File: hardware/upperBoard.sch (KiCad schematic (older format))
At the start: 23 parts, among them J1 Program interface, J2 Conn_02x10_Odd_Even, Q1 MMBT3904, Q2 MMBT3904, SW1 Reset, SW2 Prog, U1 ESP-12F, U2 A2982, U3 MCP23017_SO, U4 A2982

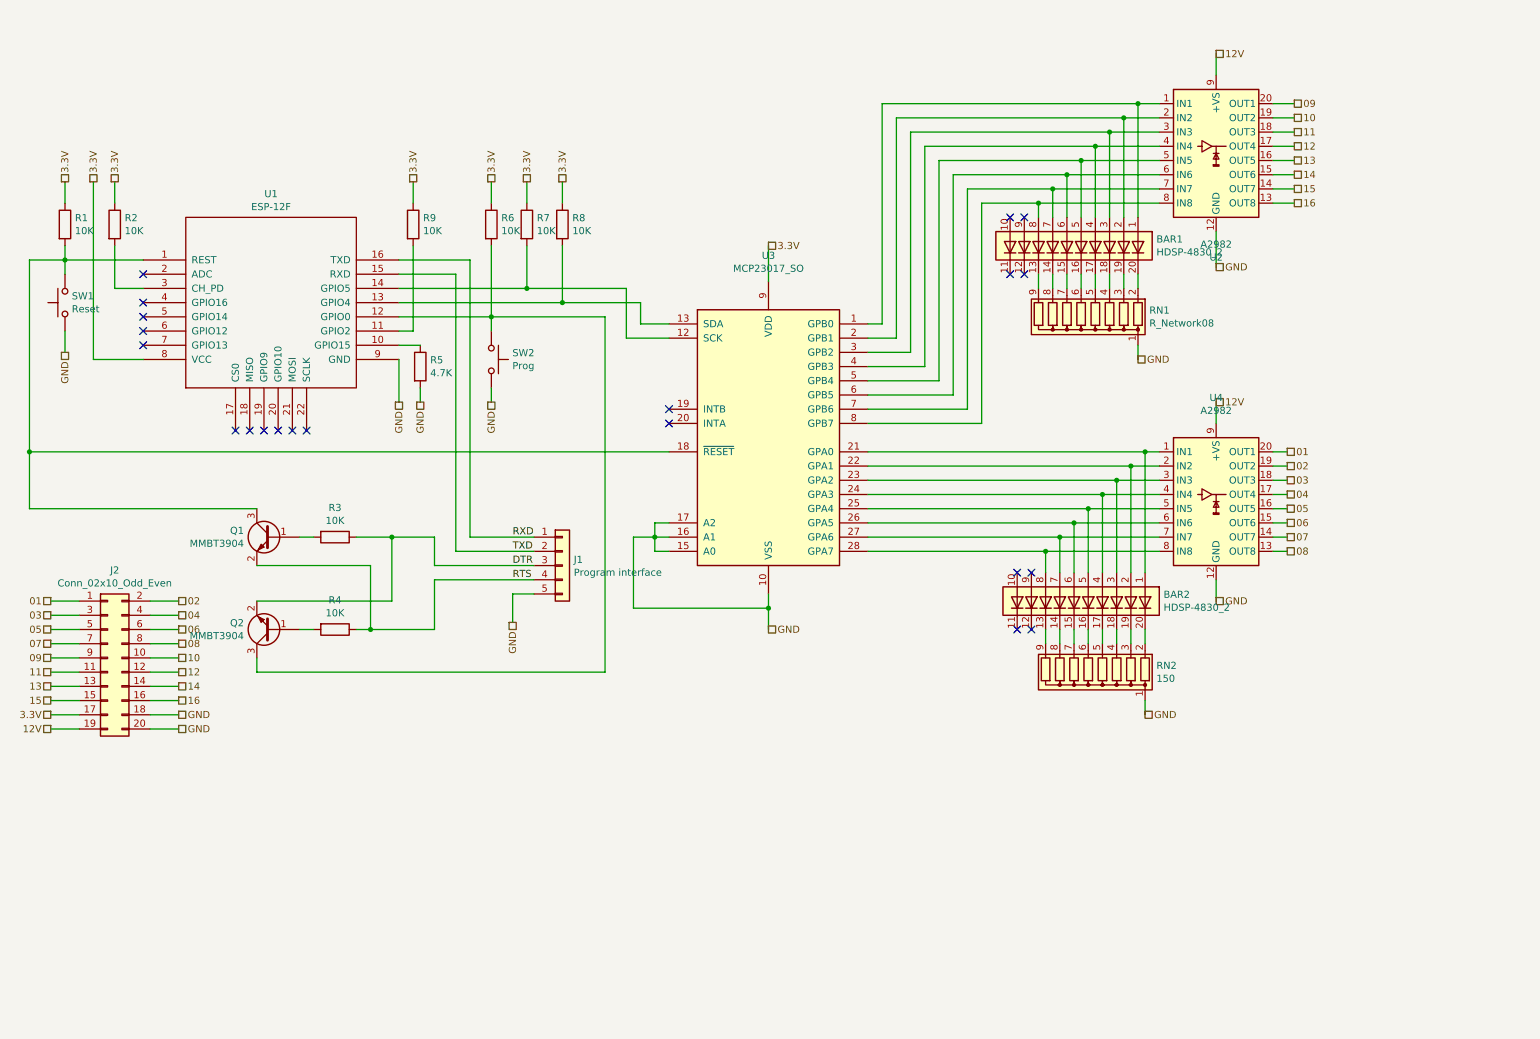
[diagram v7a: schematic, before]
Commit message: lower board fixes and started with upper printed circuit board
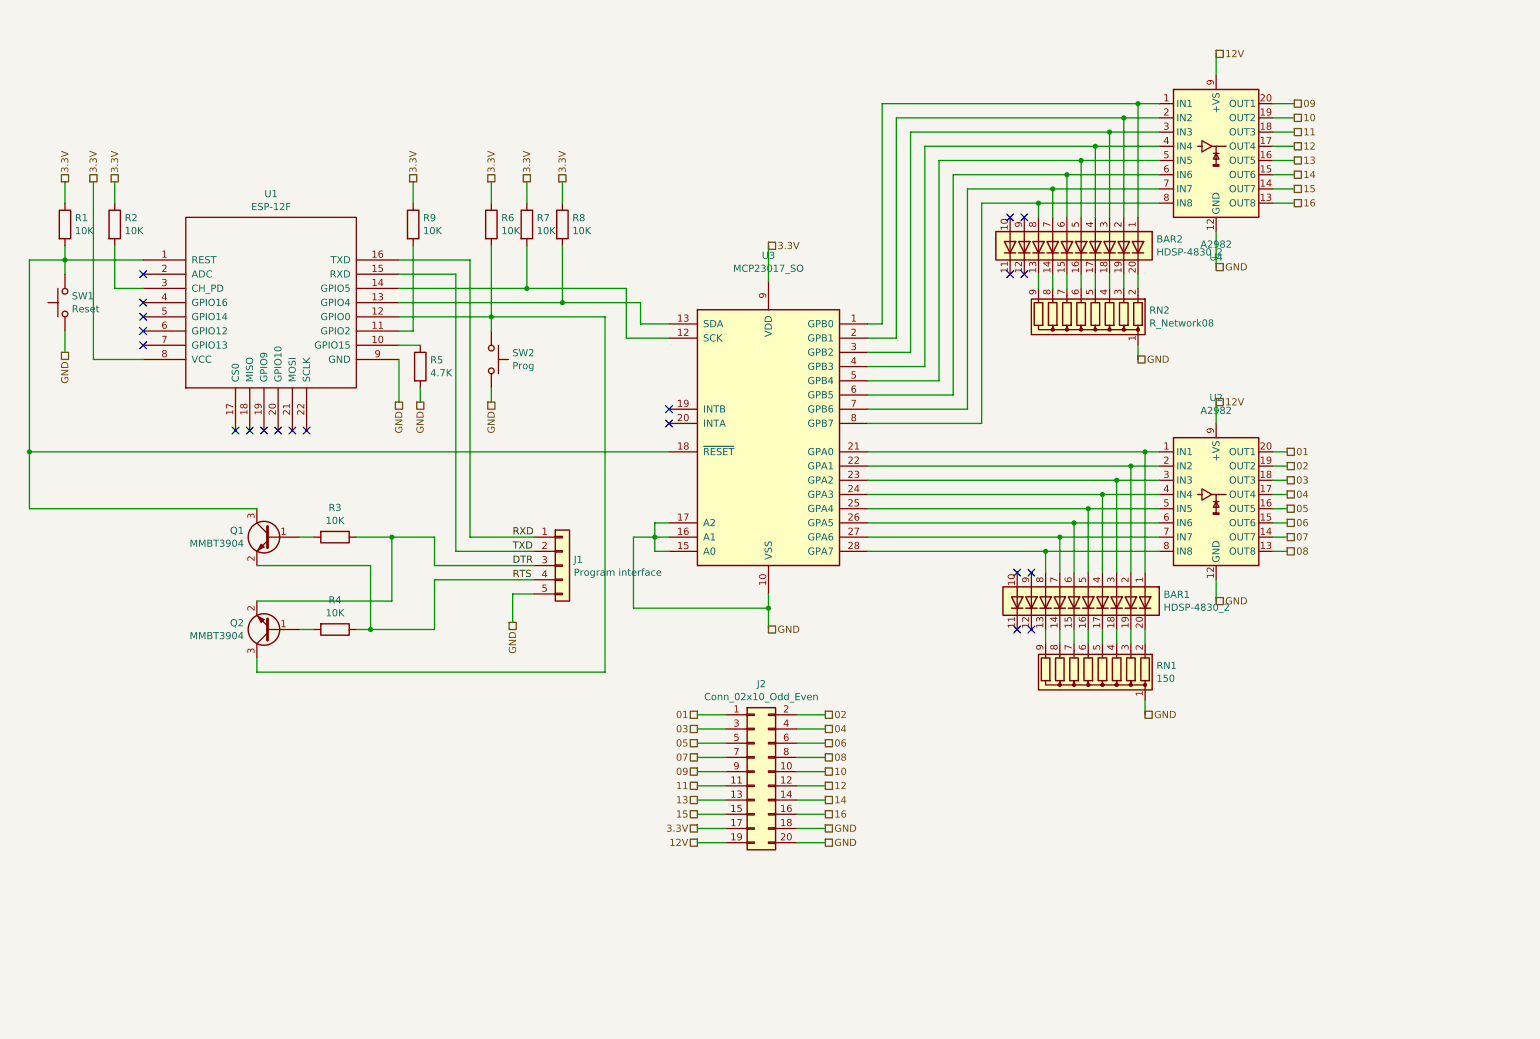
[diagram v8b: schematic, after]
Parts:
- BAR1: renamed from BAR2; footprint Display:HDSP-4830 -> Package_DIP:DIP-20_W7.62mm_LongPads
- BAR2: renamed from BAR1; footprint Display:HDSP-4830 -> Package_DIP:DIP-20_W7.62mm_Socket_LongPads
- J2: footprint (none) -> Connector_PinHeader_2.54mm:PinHeader_2x10_P2.54mm_Vertical
- renumbered RN2 to RN1, RN1 to RN2, U4 to U2, U2 to U4
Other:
- moved on the sheet: J2
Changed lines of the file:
@@
 Wire Wire Line
 	3300 2600 4450 2600
-Text HLabel 850  5500 0    50   UnSpc ~ 0
-3.3V
-Text HLabel 1750 5500 2    50   UnSpc ~ 0
+Text HLabel 5400 6300 0    50   UnSpc ~ 0
+3.3V
+Text HLabel 6300 6300 2    50   UnSpc ~ 0
 GND
 Text HLabel 3950 3300 3    50   UnSpc ~ 0
@@
 Text HLabel 4450 1750 1    50   UnSpc ~ 0
 3.3V
-Text HLabel 850  5400 0    50   UnSpc ~ 0
+Text HLabel 5400 6200 0    50   UnSpc ~ 0
 15
-Text HLabel 850  5300 0    50   UnSpc ~ 0
+Text HLabel 5400 6100 0    50   UnSpc ~ 0
 13
-Text HLabel 850  5200 0    50   UnSpc ~ 0
+Text HLabel 5400 6000 0    50   UnSpc ~ 0
 11
-Text HLabel 850  5100 0    50   UnSpc ~ 0
+Text HLabel 5400 5900 0    50   UnSpc ~ 0
 09
-Text HLabel 850  5000 0    50   UnSpc ~ 0
+Text HLabel 5400 5800 0    50   UnSpc ~ 0
 07
-Text HLabel 850  4900 0    50   UnSpc ~ 0
+Text HLabel 5400 5700 0    50   UnSpc ~ 0
 05
-Text HLabel 850  4800 0    50   UnSpc ~ 0
+Text HLabel 5400 5600 0    50   UnSpc ~ 0
 03
-Text HLabel 850  4700 0    50   UnSpc ~ 0
+Text HLabel 5400 5500 0    50   UnSpc ~ 0
 01
-Text HLabel 1750 5400 2    50   UnSpc ~ 0
+Text HLabel 6300 6200 2    50   UnSpc ~ 0
 16
-Text HLabel 1750 5300 2    50   UnSpc ~ 0
+Text HLabel 6300 6100 2    50   UnSpc ~ 0
 14
-Text HLabel 1750 5200 2    50   UnSpc ~ 0
+Text HLabel 6300 6000 2    50   UnSpc ~ 0
 12
-Text HLabel 1750 5100 2    50   UnSpc ~ 0
+Text HLabel 6300 5900 2    50   UnSpc ~ 0
 10
-Text HLabel 1750 5000 2    50   UnSpc ~ 0
+Text HLabel 6300 5800 2    50   UnSpc ~ 0
 08
-Text HLabel 1750 4900 2    50   UnSpc ~ 0
+Text HLabel 6300 5700 2    50   UnSpc ~ 0
 06
-Text HLabel 1750 4800 2    50   UnSpc ~ 0
+Text HLabel 6300 5600 2    50   UnSpc ~ 0
 04
-Text HLabel 1750 4700 2    50   UnSpc ~ 0
+Text HLabel 6300 5500 2    50   UnSpc ~ 0
 02
 Wire Wire Line
-	850  4700 1050 4700
-Wire Wire Line
-	1050 4800 850  4800
-Wire Wire Line
-	850  4900 1050 4900
-Wire Wire Line
-	1050 5000 850  5000
-Wire Wire Line
-	850  5100 1050 5100
-Wire Wire Line
-	1050 5200 850  5200
-Wire Wire Line
-	1050 5500 850  5500
-Wire Wire Line
-	1550 4700 1750 4700
-Wire Wire Line
-	1550 4800 1750 4800
-Wire Wire Line
-	1750 4900 1550 4900
-Wire Wire Line
-	1750 5000 1550 5000
-Wire Wire Line
-	1750 5100 1550 5100
-Wire Wire Line
-	1750 5200 1550 5200
-Wire Wire Line
-	1750 5300 1550 5300
-Wire Wire Line
-	1750 5400 1550 5400
+	5400 5500 5600 5500
+Wire Wire Line
+	5600 5600 5400 5600
+Wire Wire Line
+	5400 5700 5600 5700
+Wire Wire Line
+	5600 5800 5400 5800
+Wire Wire Line
+	5400 5900 5600 5900
+Wire Wire Line
+	5600 6000 5400 6000
+Wire Wire Line
+	5600 6300 5400 6300
+Wire Wire Line
+	6100 5500 6300 5500
+Wire Wire Line
+	6100 5600 6300 5600
+Wire Wire Line
+	6300 5700 6100 5700
+Wire Wire Line
+	6300 5800 6100 5800
+Wire Wire Line
+	6300 5900 6100 5900
+Wire Wire Line
+	6300 6000 6100 6000
+Wire Wire Line
+	6300 6100 6100 6100
+Wire Wire Line
+	6300 6200 6100 6200
 Text HLabel 9600 1900 2    50   UnSpc ~ 0
 16
 Wire Wire Line
-	1050 5300 850  5300
-Wire Wire Line
-	1050 5400 850  5400
-Wire Wire Line
-	1550 5500 1750 5500
-$Comp
-L LED:HDSP-4830_2 BAR2
+	5600 6100 5400 6100
+Wire Wire Line
+	5600 6200 5400 6200
+Wire Wire Line
+	6100 6300 6300 6300
+$Comp
+L LED:HDSP-4830_2 BAR1
 U 1 1 5D99BD45
 P 8150 4700
-F 0 "BAR2" V 8104 5230 50  0000 L CNN
+F 0 "BAR1" V 8104 5230 50  0000 L CNN
 F 1 "HDSP-4830_2" V 8195 5230 50  0000 L CNN
-F 2 "Display:HDSP-4830" H 8150 3900 50  0001 C CNN
+F 2 "Package_DIP:DIP-20_W7.62mm_LongPads" H 8150 3900 50  0001 C CNN
 F 3 "https://docs.broadcom.com/docs/AV02-1798EN" H 6150 4900 50  0001 C CNN
 	1    8150 4700
@@
 $EndComp
 $Comp
-L Device:R_Network08 RN2
+L Device:R_Network08 RN1
 U 1 1 5D99E6B0
 P 8150 5200
-F 0 "RN2" H 7670 5154 50  0000 R CNN
+F 0 "RN1" H 7670 5154 50  0000 R CNN
 F 1 "150" H 7670 5245 50  0000 R CNN
 F 2 "Resistor_THT:R_Array_SIP9" V 8625 5200 50  0001 C CNN
@@
 	8650 3750 8450 3750
 $Comp
-L Transistor_Array:A2982 U4
+L Transistor_Array:A2982 U2
 U 1 1 5D997ACC
 P 9050 3950
-F 0 "U4" H 9050 4631 50  0000 C CNN
+F 0 "U2" H 9050 4631 50  0000 C CNN
 F 1 "A2982" H 9050 4540 50  0000 C CNN
 F 2 "Package_SO:SOIC-20W_7.5x12.8mm_P1.27mm" H 9050 3400 50  0001 C CNN
@@
 $EndComp
 $Comp
-L Transistor_Array:A2982 U2
+L Transistor_Array:A2982 U4
 U 1 1 5D9A699E
 P 9050 1500
-F 0 "U2" H 9050 719 50  0000 C CNN
+F 0 "U4" H 9050 719 50  0000 C CNN
 F 1 "A2982" H 9050 810 50  0000 C CNN
 F 2 "Package_SO:SOIC-20W_7.5x12.8mm_P1.27mm" H 9050 950 50  0001 C CNN
@@
 $EndComp
 $Comp
-L LED:HDSP-4830_2 BAR1
+L LED:HDSP-4830_2 BAR2
 U 1 1 5D9A7C3A
 P 8100 2200
-F 0 "BAR1" V 8054 2730 50  0000 L CNN
+F 0 "BAR2" V 8054 2730 50  0000 L CNN
 F 1 "HDSP-4830_2" V 8145 2730 50  0000 L CNN
-F 2 "Display:HDSP-4830" H 8100 1400 50  0001 C CNN
+F 2 "Package_DIP:DIP-20_W7.62mm_Socket_LongPads" H 8100 1400 50  0001 C CNN
 F 3 "https://docs.broadcom.com/docs/AV02-1798EN" H 6100 2400 50  0001 C CNN
 	1    8100 2200
@@
 $EndComp
 $Comp
-L Device:R_Network08 RN1
+L Device:R_Network08 RN2
 U 1 1 5D9A9ED4
 P 8100 2700
-F 0 "RN1" H 7620 2654 50  0000 R CNN
+F 0 "RN2" H 7620 2654 50  0000 R CNN
 F 1 "R_Network08" H 7620 2745 50  0000 R CNN
 F 2 "Resistor_THT:R_Array_SIP9" V 8575 2700 50  0001 C CNN
@@
 L Connector_Generic:Conn_02x10_Odd_Even J2
 U 1 1 5DAC3666
-P 1250 5100
-F 0 "J2" H 1300 5717 50  0000 C CNN
-F 1 "Conn_02x10_Odd_Even" H 1300 5626 50  0000 C CNN
-F 2 "" H 1250 5100 50  0001 C CNN
-F 3 "~" H 1250 5100 50  0001 C CNN
-	1    1250 5100
+P 5800 5900
+F 0 "J2" H 5850 6517 50  0000 C CNN
+F 1 "Conn_02x10_Odd_Even" H 5850 6426 50  0000 C CNN
+F 2 "Connector_PinHeader_2.54mm:PinHeader_2x10_P2.54mm_Vertical" H 5800 5900 50  0001 C CNN
+F 3 "~" H 5800 5900 50  0001 C CNN
+	1    5800 5900
 	1    0    0    -1
 $EndComp
-Text HLabel 1750 5600 2    50   UnSpc ~ 0
-GND
-Wire Wire Line
-	1750 5600 1550 5600
-Text HLabel 850  5600 0    50   UnSpc ~ 0
+Text HLabel 6300 6400 2    50   UnSpc ~ 0
+GND
+Wire Wire Line
+	6300 6400 6100 6400
+Text HLabel 5400 6400 0    50   UnSpc ~ 0
 12V
 Wire Wire Line
-	1050 5600 850  5600
+	5600 6400 5400 6400
 Text HLabel 9050 850  2    50   UnSpc ~ 0
 12V
